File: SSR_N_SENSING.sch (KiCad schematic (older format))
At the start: 26 parts, among them P4 CONN_01X03, P7 CONN_01X02, P8 CONN_01X02, Q1 BC850, U10 ACS722, U3 SHARPS202S02, U4 ACS716

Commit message: PWR layout
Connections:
- net labels added: 230VPHASE
- net labels removed: 220VPHASE
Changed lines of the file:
@@
 CURR_SENSE_FILTERED
 Text GLabel 4200 2500 2    60   Input ~ 0
-220VPHASE
+230VPHASE
 $Comp
 L ACS722 U10

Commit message: almost ready
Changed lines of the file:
@@
 	1    0    0    -1
 $EndComp
-Wire Wire Line
-	3450 3200 3450 4350
-Connection ~ 3450 3300
-Connection ~ 3450 3400
-Wire Wire Line
-	3450 2500 3450 3100
-Connection ~ 3450 3000
-Connection ~ 3450 2900
-Connection ~ 3450 2800
-Wire Wire Line
-	3450 2400 4200 2400
 $Comp
 L R R13
@@
 	0    1    1    0
 $EndComp
-Wire Wire Line
-	3450 2500 3500 2500
-Wire Wire Line
-	3800 2500 3850 2500
-Wire Wire Line
-	4150 2500 4200 2500
 $Comp
 L GNDREF #PWR038
@@
 	0    1    1    0
 $EndComp
-Wire Wire Line
-	4200 2500 4200 2400
-Wire Wire Line
-	3450 2200 3550 2200
 $Comp
 L GNDREF #PWR040
@@
 	-1   0    0    1
 $EndComp
-Wire Wire Line
-	3550 2200 3550 2000
-Wire Wire Line
-	3550 2000 3700 2000
 $Comp
 L D D6
@@
 	0    -1   -1   0
 $EndComp
-Wire Wire Line
-	3650 2300 3450 2300
 $Comp
 L R R14
@@
 	-1   0    0    1
 $EndComp
-Wire Wire Line
-	4950 2900 5850 2900
-Connection ~ 5700 2900
-Wire Wire Line
-	4950 2900 4950 3000
 $Comp
 L GNDREF #PWR042
@@
 	1    0    0    -1
 $EndComp
-Wire Wire Line
-	5550 3300 4950 3300
 $Comp
 L C C11
@@
 	1    0    0    -1
 $EndComp
-Wire Wire Line
-	5300 3400 4950 3400
 Text HLabel 4950 2800 2    60   Input ~ 0
 FAULT_EN
 Text HLabel 4950 3100 2    60   Input ~ 0
 !FAULT
-Wire Wire Line
-	4950 3200 6250 3200
 $Comp
 L D D7
@@
 	1    0    0    -1
 $EndComp
-Wire Wire Line
-	6100 3500 6350 3500
-Connection ~ 6200 3500
 $Comp
 L GNDREF #PWR045
@@
 	1    0    0    -1
 $EndComp
-Wire Wire Line
-	6200 3800 6350 3800
-Wire Wire Line
-	6350 3800 6350 3900
 Text HLabel 6350 3500 2    60   Input ~ 0
 CURR_SENSE_FILTERED
@@
 	1    0    0    -1
 $EndComp
-Wire Wire Line
-	3450 4450 3450 4550
-Connection ~ 3450 3500
-Connection ~ 3450 4250
 $Comp
 L GNDREF #PWR046
@@
 	1    0    0    -1
 $EndComp
-Wire Wire Line
-	4950 4250 7400 4250
 $Comp
 L C C22
@@
 	1    0    0    -1
 $EndComp
-Wire Wire Line
-	6100 5050 6350 5050
-Connection ~ 6200 5050
 $Comp
 L GNDREF #PWR050
@@
 	1    0    0    -1
 $EndComp
-Wire Wire Line
-	6200 5350 6350 5350
-Wire Wire Line
-	6350 5350 6350 5450
 Text HLabel 6350 5050 2    60   Input ~ 0
 CURR_SENSE_FILTERED_2
@@
 	1    0    0    -1
 $EndComp
-Wire Wire Line
-	4950 4450 5150 4450
 $Comp
 L GNDREF #PWR051
@@
 	1    0    0    -1
 $EndComp
-Text HLabel 6300 4750 2    60   Input ~ 0
+Text HLabel 6100 4700 2    60   Input ~ 0
 CURR_SENSE_DIRECT_2
 $Comp
@@
 	1    0    0    -1
 $EndComp
-Wire Wire Line
-	4950 4350 5700 4350
-Connection ~ 5450 4350
-Wire Wire Line
-	5700 4650 5700 4750
-Wire Wire Line
-	5700 4700 6100 4700
-Connection ~ 5700 4700
-Wire Wire Line
-	6100 4700 6100 4750
 $Comp
 L CONN_01X02 P7
@@
 	-1   0    0    1
 $EndComp
-Wire Wire Line
-	3450 3100 3300 3100
-Wire Wire Line
-	3300 3200 3450 3200
 $Comp
 L CONN_01X02 P8
@@
 $EndComp
 Wire Wire Line
+	3450 3200 3450 4350
+Connection ~ 3450 3300
+Connection ~ 3450 3400
+Wire Wire Line
+	3450 2500 3450 3100
+Connection ~ 3450 3000
+Connection ~ 3450 2900
+Connection ~ 3450 2800
+Wire Wire Line
+	3450 2400 4200 2400
+Wire Wire Line
+	3450 2500 3500 2500
+Wire Wire Line
+	3800 2500 3850 2500
+Wire Wire Line
+	4150 2500 4200 2500
+Wire Wire Line
+	4200 2500 4200 2400
+Wire Wire Line
+	3450 2200 3550 2200
+Wire Wire Line
+	3550 2200 3550 2000
+Wire Wire Line
+	3550 2000 3700 2000
+Wire Wire Line
+	3650 2300 3450 2300
+Wire Wire Line
+	4950 2900 5850 2900
+Connection ~ 5700 2900
+Wire Wire Line
+	4950 2900 4950 3000
+Wire Wire Line
+	5550 3300 4950 3300
+Wire Wire Line
+	5300 3400 4950 3400
+Wire Wire Line
+	6100 3500 6350 3500
+Connection ~ 6200 3500
+Wire Wire Line
+	6200 3800 6350 3800
+Wire Wire Line
+	6350 3800 6350 3900
+Wire Wire Line
+	3450 4450 3450 4550
+Connection ~ 3450 3500
+Connection ~ 3450 4250
+Wire Wire Line
+	4950 4250 7400 4250
+Wire Wire Line
+	6100 5050 6350 5050
+Connection ~ 6200 5050
+Wire Wire Line
+	6200 5350 6350 5350
+Wire Wire Line
+	6350 5350 6350 5450
+Wire Wire Line
+	4950 4450 5150 4450
+Wire Wire Line
+	4950 4350 5700 4350
+Connection ~ 5450 4350
+Wire Wire Line
+	5700 4650 5700 4750
+Wire Wire Line
+	5700 4700 6100 4700
+Connection ~ 5700 4700
+Wire Wire Line
+	6100 4700 6100 4750
+Wire Wire Line
+	3450 3100 3300 3100
+Wire Wire Line
+	3300 3200 3450 3200
+Wire Wire Line
 	3450 4350 3300 4350
 Wire Wire Line
 	3300 4450 3450 4450
+Connection ~ 3650 2000
+Wire Wire Line
+	4950 3200 6250 3200
+Connection ~ 6100 3200
 $EndSCHEMATC

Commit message: maybe final
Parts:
- D6, D7, D8: footprint Diodes_SMD:DO-214AB_Handsoldering -> Diodes_SMD:SOD-123
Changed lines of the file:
@@
 F 0 "D6" H 3650 2250 50  0000 C CNN
 F 1 "D" H 3650 2050 50  0000 C CNN
-F 2 "Diodes_SMD:DO-214AB_Handsoldering" H 3650 2150 60  0001 C CNN
+F 2 "Diodes_SMD:SOD-123" H 3650 2150 60  0001 C CNN
 F 3 "" H 3650 2150 60  0000 C CNN
 	1    3650 2150
@@
 F 0 "D7" H 6100 3450 50  0000 C CNN
 F 1 "D" H 6100 3250 50  0000 C CNN
-F 2 "Diodes_SMD:DO-214AB_Handsoldering" H 6100 3350 60  0001 C CNN
+F 2 "Diodes_SMD:SOD-123" H 6100 3350 60  0001 C CNN
 F 3 "" H 6100 3350 60  0000 C CNN
 	1    6100 3350
@@
 F 0 "D8" H 6100 5000 50  0000 C CNN
 F 1 "D" H 6100 4800 50  0000 C CNN
-F 2 "Diodes_SMD:DO-214AB_Handsoldering" H 6100 4900 60  0001 C CNN
+F 2 "Diodes_SMD:SOD-123" H 6100 4900 60  0001 C CNN
 F 3 "" H 6100 4900 60  0000 C CNN
 	1    6100 4900

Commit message: printed version
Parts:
- R13: footprint Resistors_ThroughHole:Resistor_Horizontal_RM25mm -> Resistors_ThroughHole:Resistor_Horizontal_RM10mm
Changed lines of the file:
@@
 F 0 "R13" V 3730 2500 50  0000 C CNN
 F 1 "R_SNUB" V 3650 2500 50  0000 C CNN
-F 2 "Resistors_ThroughHole:Resistor_Horizontal_RM25mm" V 3580 2500 30  0001 C CNN
+F 2 "Resistors_ThroughHole:Resistor_Horizontal_RM10mm" V 3580 2500 30  0001 C CNN
 F 3 "" H 3650 2500 30  0000 C CNN
 	1    3650 2500

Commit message: save
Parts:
- removed C11, C12, C13, C14: C, Capacitors_SMD:C_1206_HandSoldering, symbol C
- removed D7: D, Diodes_SMD:SOD-123, symbol D
- removed P7: CONN_01X02, libs:PIN_CONN_0.3Inch, symbol CONN_01X02
- removed R16: R, Resistors_SMD:R_1206_HandSoldering, symbol R
- removed U4: ACS716, libs:ACS716, symbol ACS716
- C20: value C -> 10uF
- C21: value C -> 1nF
- C22: value C -> 0; footprint Capacitors_SMD:C_1206_HandSoldering -> 0
- C23: value C -> 10uF; footprint Capacitors_SMD:C_1206_HandSoldering -> 10uF
- R14: value R -> 150
- R15: value R -> 1k
- R17: value R -> 2k
- R18: value R -> 3k
- R19: value R -> 100k; footprint Resistors_SMD:R_1206_HandSoldering -> 100k
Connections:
- net labels removed: !FAULT, CURR_SENSE_DIRECT, CURR_SENSE_FILTERED, FAULT_EN
- wire segments 33 -> 22
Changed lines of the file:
@@
 EESchema Schematic File Version 2
+LIBS:viztisztito-rescue
 LIBS:power
 LIBS:device
@@
 MOTOR+
 $Comp
-L ACS716 U4
-U 1 1 561BA190
-P 4200 3150
-F 0 "U4" H 4200 3050 50  0000 C CNN
-F 1 "ACS716" H 4200 3250 50  0000 C CNN
-F 2 "libs:ACS716" H 4200 3150 50  0001 C CNN
-F 3 "DOCUMENTATION" H 4200 3150 50  0001 C CNN
-	1    4200 3150
-	1    0    0    -1
-$EndComp
-$Comp
 L R R13
 U 1 1 561BB7FA
@@
 $EndComp
 $Comp
-L GNDREF #PWR038
-U 1 1 561BB966
-P 4950 3500
-F 0 "#PWR038" H 4950 3250 50  0001 C CNN
-F 1 "GNDREF" H 4950 3350 50  0000 C CNN
-F 2 "" H 4950 3500 60  0000 C CNN
-F 3 "" H 4950 3500 60  0000 C CNN
-	1    4950 3500
-	1    0    0    -1
-$EndComp
-$Comp
-L +3.3V #PWR039
-U 1 1 561BB9CA
-P 5850 2900
-F 0 "#PWR039" H 5850 2750 50  0001 C CNN
-F 1 "+3.3V" H 5850 3040 50  0000 C CNN
-F 2 "" H 5850 2900 60  0000 C CNN
-F 3 "" H 5850 2900 60  0000 C CNN
-	1    5850 2900
-	0    1    1    0
-$EndComp
-$Comp
 L GNDREF #PWR040
 U 1 1 561BC35A
@@
 P 3800 2300
 F 0 "R14" V 3880 2300 50  0000 C CNN
-F 1 "R" V 3800 2300 50  0000 C CNN
+F 1 "150" V 3800 2300 50  0000 C CNN
 F 2 "Resistors_SMD:R_1206_HandSoldering" V 3730 2300 30  0001 C CNN
 F 3 "" H 3800 2300 30  0000 C CNN
@@
 P 4150 1800
 F 0 "R15" V 4230 1800 50  0000 C CNN
-F 1 "R" V 4150 1800 50  0000 C CNN
+F 1 "1k" V 4150 1800 50  0000 C CNN
 F 2 "Resistors_SMD:R_1206_HandSoldering" V 4080 1800 30  0001 C CNN
 F 3 "" H 4150 1800 30  0000 C CNN
@@
 	-1   0    0    1
 $EndComp
-Text HLabel 6250 3200 2    60   Input ~ 0
-CURR_SENSE_DIRECT
-$Comp
-L C C13
-U 1 1 561BD266
-P 5700 2750
-F 0 "C13" H 5725 2850 50  0000 L CNN
-F 1 "C" H 5725 2650 50  0000 L CNN
-F 2 "Capacitors_SMD:C_1206_HandSoldering" H 5738 2600 30  0001 C CNN
-F 3 "" H 5700 2750 60  0000 C CNN
-	1    5700 2750
-	-1   0    0    1
-$EndComp
-$Comp
-L GNDREF #PWR042
-U 1 1 561BD41D
-P 5700 2600
-F 0 "#PWR042" H 5700 2350 50  0001 C CNN
-F 1 "GNDREF" H 5700 2450 50  0000 C CNN
-F 2 "" H 5700 2600 60  0000 C CNN
-F 3 "" H 5700 2600 60  0000 C CNN
-	1    5700 2600
-	-1   0    0    1
-$EndComp
-$Comp
-L C C12
-U 1 1 561BD44D
-P 5550 3450
-F 0 "C12" H 5575 3550 50  0000 L CNN
-F 1 "C" H 5575 3350 50  0000 L CNN
-F 2 "Capacitors_SMD:C_1206_HandSoldering" H 5588 3300 30  0001 C CNN
-F 3 "" H 5550 3450 60  0000 C CNN
-	1    5550 3450
-	1    0    0    -1
-$EndComp
-$Comp
-L GNDREF #PWR043
-U 1 1 561BD495
-P 5550 3600
-F 0 "#PWR043" H 5550 3350 50  0001 C CNN
-F 1 "GNDREF" H 5550 3450 50  0000 C CNN
-F 2 "" H 5550 3600 60  0000 C CNN
-F 3 "" H 5550 3600 60  0000 C CNN
-	1    5550 3600
-	1    0    0    -1
-$EndComp
-$Comp
-L C C11
-U 1 1 561BD4EE
-P 5300 3550
-F 0 "C11" H 5325 3650 50  0000 L CNN
-F 1 "C" H 5325 3450 50  0000 L CNN
-F 2 "Capacitors_SMD:C_1206_HandSoldering" H 5338 3400 30  0001 C CNN
-F 3 "" H 5300 3550 60  0000 C CNN
-	1    5300 3550
-	1    0    0    -1
-$EndComp
-$Comp
-L GNDREF #PWR044
-U 1 1 561BD527
-P 5300 3700
-F 0 "#PWR044" H 5300 3450 50  0001 C CNN
-F 1 "GNDREF" H 5300 3550 50  0000 C CNN
-F 2 "" H 5300 3700 60  0000 C CNN
-F 3 "" H 5300 3700 60  0000 C CNN
-	1    5300 3700
-	1    0    0    -1
-$EndComp
-Text HLabel 4950 2800 2    60   Input ~ 0
-FAULT_EN
-Text HLabel 4950 3100 2    60   Input ~ 0
-!FAULT
-$Comp
-L D D7
-U 1 1 561BF7C0
-P 6100 3350
-F 0 "D7" H 6100 3450 50  0000 C CNN
-F 1 "D" H 6100 3250 50  0000 C CNN
-F 2 "Diodes_SMD:SOD-123" H 6100 3350 60  0001 C CNN
-F 3 "" H 6100 3350 60  0000 C CNN
-	1    6100 3350
-	0    -1   -1   0
-$EndComp
-$Comp
-L R R16
-U 1 1 561BF888
-P 6200 3650
-F 0 "R16" V 6280 3650 50  0000 C CNN
-F 1 "R" V 6200 3650 50  0000 C CNN
-F 2 "Resistors_SMD:R_1206_HandSoldering" V 6130 3650 30  0001 C CNN
-F 3 "" H 6200 3650 30  0000 C CNN
-	1    6200 3650
-	-1   0    0    1
-$EndComp
-$Comp
-L C C14
-U 1 1 561BF95E
-P 6350 3650
-F 0 "C14" H 6375 3750 50  0000 L CNN
-F 1 "C" H 6375 3550 50  0000 L CNN
-F 2 "Capacitors_SMD:C_1206_HandSoldering" H 6388 3500 30  0001 C CNN
-F 3 "" H 6350 3650 60  0000 C CNN
-	1    6350 3650
-	1    0    0    -1
-$EndComp
-$Comp
-L GNDREF #PWR045
-U 1 1 561BFC0A
-P 6350 3900
-F 0 "#PWR045" H 6350 3650 50  0001 C CNN
-F 1 "GNDREF" H 6350 3750 50  0000 C CNN
-F 2 "" H 6350 3900 60  0000 C CNN
-F 3 "" H 6350 3900 60  0000 C CNN
-	1    6350 3900
-	1    0    0    -1
-$EndComp
-Text HLabel 6350 3500 2    60   Input ~ 0
-CURR_SENSE_FILTERED
 Text GLabel 4200 2500 2    60   Input ~ 0
 230VPHASE
@@
 P 4950 4100
 F 0 "C20" H 4975 4200 50  0000 L CNN
-F 1 "C" H 4975 4000 50  0000 L CNN
+F 1 "10uF" H 4975 4000 50  0000 L CNN
 F 2 "Capacitors_SMD:C_1206_HandSoldering" H 4988 3950 30  0001 C CNN
 F 3 "" H 4950 4100 60  0000 C CNN
@@
 P 5450 4500
 F 0 "C22" H 5475 4600 50  0000 L CNN
-F 1 "C" H 5475 4400 50  0000 L CNN
-F 2 "Capacitors_SMD:C_1206_HandSoldering" H 5488 4350 30  0001 C CNN
+F 1 "0" H 5475 4400 50  0000 L CNN
+F 2 "0" H 5488 4350 30  0001 C CNN
 F 3 "" H 5450 4500 60  0000 C CNN
 	1    5450 4500
@@
 P 6200 5200
 F 0 "R19" V 6280 5200 50  0000 C CNN
-F 1 "R" V 6200 5200 50  0000 C CNN
-F 2 "Resistors_SMD:R_1206_HandSoldering" V 6130 5200 30  0001 C CNN
+F 1 "100k" V 6200 5200 50  0000 C CNN
+F 2 "100k" V 6130 5200 30  0001 C CNN
 F 3 "" H 6200 5200 30  0000 C CNN
 	1    6200 5200
@@
 P 6350 5200
 F 0 "C23" H 6375 5300 50  0000 L CNN
-F 1 "C" H 6375 5100 50  0000 L CNN
-F 2 "Capacitors_SMD:C_1206_HandSoldering" H 6388 5050 30  0001 C CNN
+F 1 "10uF" H 6375 5100 50  0000 L CNN
+F 2 "10uF" H 6388 5050 30  0001 C CNN
 F 3 "" H 6350 5200 60  0000 C CNN
 	1    6350 5200
@@
 P 5150 4600
 F 0 "C21" H 5175 4700 50  0000 L CNN
-F 1 "C" H 5175 4500 50  0000 L CNN
+F 1 "1nF" H 5175 4500 50  0000 L CNN
 F 2 "Capacitors_SMD:C_1206_HandSoldering" H 5188 4450 30  0001 C CNN
 F 3 "" H 5150 4600 60  0000 C CNN
@@
 P 5700 4500
 F 0 "R17" V 5780 4500 50  0000 C CNN
-F 1 "R" V 5700 4500 50  0000 C CNN
+F 1 "2k" V 5700 4500 50  0000 C CNN
 F 2 "Resistors_SMD:R_1206_HandSoldering" V 5630 4500 30  0001 C CNN
 F 3 "" H 5700 4500 30  0000 C CNN
@@
 P 5700 4900
 F 0 "R18" V 5780 4900 50  0000 C CNN
-F 1 "R" V 5700 4900 50  0000 C CNN
+F 1 "3k" V 5700 4900 50  0000 C CNN
 F 2 "Resistors_SMD:R_1206_HandSoldering" V 5630 4900 30  0001 C CNN
 F 3 "" H 5700 4900 30  0000 C CNN
@@
 $EndComp
 $Comp
-L CONN_01X02 P7
-U 1 1 5626DC35
-P 3100 3150
-F 0 "P7" H 3100 3300 50  0000 C CNN
-F 1 "CONN_01X02" V 3200 3150 50  0000 C CNN
-F 2 "libs:PIN_CONN_0.3Inch" H 3100 3150 60  0000 C CNN
-F 3 "" H 3100 3150 60  0000 C CNN
-	1    3100 3150
-	-1   0    0    1
-$EndComp
-$Comp
 L CONN_01X02 P8
 U 1 1 5626DE5E
@@
 $EndComp
 Wire Wire Line
-	3450 3200 3450 4350
-Connection ~ 3450 3300
-Connection ~ 3450 3400
-Wire Wire Line
-	3450 2500 3450 3100
-Connection ~ 3450 3000
-Connection ~ 3450 2900
-Connection ~ 3450 2800
-Wire Wire Line
 	3450 2400 4200 2400
 Wire Wire Line
@@
 	3650 2300 3450 2300
 Wire Wire Line
-	4950 2900 5850 2900
-Connection ~ 5700 2900
-Wire Wire Line
-	4950 2900 4950 3000
-Wire Wire Line
-	5550 3300 4950 3300
-Wire Wire Line
-	5300 3400 4950 3400
-Wire Wire Line
-	6100 3500 6350 3500
-Connection ~ 6200 3500
-Wire Wire Line
-	6200 3800 6350 3800
-Wire Wire Line
-	6350 3800 6350 3900
-Wire Wire Line
 	3450 4450 3450 4550
-Connection ~ 3450 3500
 Connection ~ 3450 4250
 Wire Wire Line
@@
 	6100 4700 6100 4750
 Wire Wire Line
-	3450 3100 3300 3100
-Wire Wire Line
-	3300 3200 3450 3200
-Wire Wire Line
 	3450 4350 3300 4350
 Wire Wire Line
@@
 Connection ~ 3650 2000
 Wire Wire Line
-	4950 3200 6250 3200
-Connection ~ 6100 3200
+	3450 4250 3450 2500
 $EndSCHEMATC

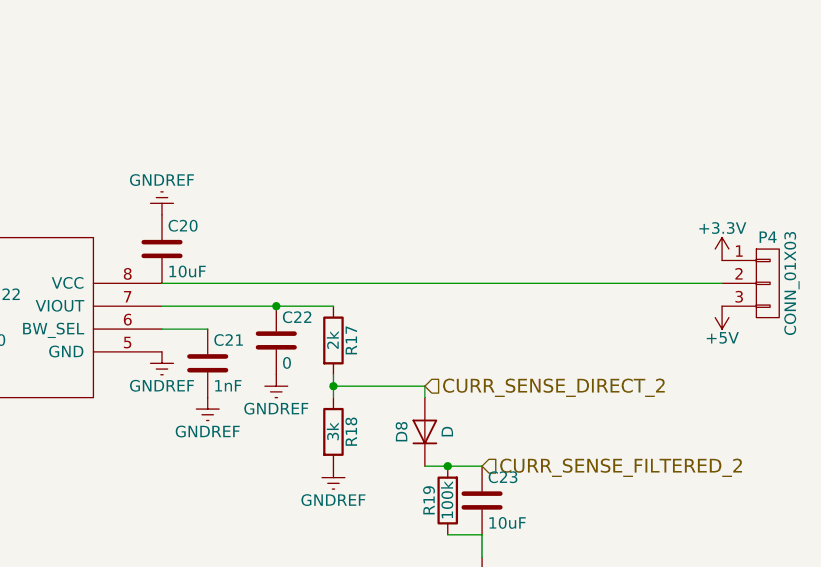
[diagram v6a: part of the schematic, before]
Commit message: new layout, added psu
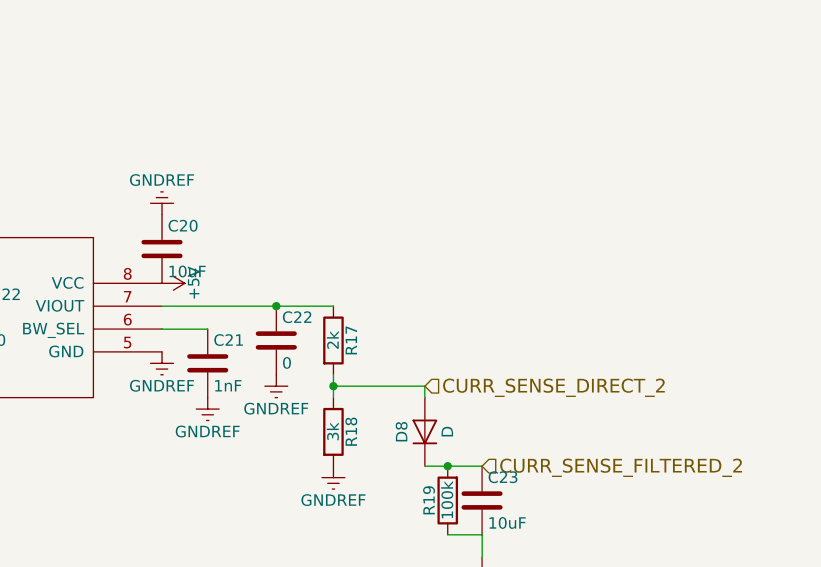
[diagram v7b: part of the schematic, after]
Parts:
- removed P4: CONN_01X03, Socket_Strips:Socket_Strip_Straight_1x03, symbol CONN_01X03
- C22: footprint 0 -> Capacitors_SMD:C_1206_HandSoldering
- C23: footprint 10uF -> Capacitors_SMD:C_1206_HandSoldering
- R19: footprint 100k -> Resistors_SMD:R_1206_HandSoldering
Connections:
- net +5V: now also C20.2, U10.8 (VCC)
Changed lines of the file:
@@
 LIBS:contrib
 LIBS:valves
-LIBS:mylib
+LIBS:analog_devices
+LIBS:libs
 LIBS:viztisztito-cache
 EELAYER 25 0
@@
 $EndComp
 $Comp
-L GNDREF #PWR040
+L GNDREF #PWR026
 U 1 1 561BC35A
 P 3700 1600
-F 0 "#PWR040" H 3700 1350 50  0001 C CNN
+F 0 "#PWR026" H 3700 1350 50  0001 C CNN
 F 1 "GNDREF" H 3700 1450 50  0000 C CNN
 F 2 "" H 3700 1600 60  0000 C CNN
@@
 $EndComp
 $Comp
-L +3.3V #PWR041
+L +3.3V #PWR027
 U 1 1 561BC509
 P 3950 2300
-F 0 "#PWR041" H 3950 2150 50  0001 C CNN
+F 0 "#PWR027" H 3950 2150 50  0001 C CNN
 F 1 "+3.3V" H 3950 2440 50  0000 C CNN
 F 2 "" H 3950 2300 60  0000 C CNN
@@
 $EndComp
 $Comp
-L GNDREF #PWR046
+L GNDREF #PWR028
 U 1 1 5625123B
 P 4950 4550
-F 0 "#PWR046" H 4950 4300 50  0001 C CNN
+F 0 "#PWR028" H 4950 4300 50  0001 C CNN
 F 1 "GNDREF" H 4950 4400 50  0000 C CNN
 F 2 "" H 4950 4550 60  0000 C CNN
@@
 $EndComp
 $Comp
-L GNDREF #PWR047
+L GNDREF #PWR029
 U 1 1 56251330
 P 4950 3950
-F 0 "#PWR047" H 4950 3700 50  0001 C CNN
+F 0 "#PWR029" H 4950 3700 50  0001 C CNN
 F 1 "GNDREF" H 4950 3800 50  0000 C CNN
 F 2 "" H 4950 3950 60  0000 C CNN
@@
 	1    4950 3950
 	-1   0    0    1
-$EndComp
-$Comp
-L +3.3V #PWR048
-U 1 1 5625147B
-P 7400 4150
-F 0 "#PWR048" H 7400 4000 50  0001 C CNN
-F 1 "+3.3V" H 7400 4290 50  0000 C CNN
-F 2 "" H 7400 4150 60  0000 C CNN
-F 3 "" H 7400 4150 60  0000 C CNN
-	1    7400 4150
-	1    0    0    -1
 $EndComp
 $Comp
@@
 F 0 "C22" H 5475 4600 50  0000 L CNN
 F 1 "0" H 5475 4400 50  0000 L CNN
-F 2 "0" H 5488 4350 30  0001 C CNN
+F 2 "Capacitors_SMD:C_1206_HandSoldering" H 5488 4350 30  0001 C CNN
 F 3 "" H 5450 4500 60  0000 C CNN
 	1    5450 4500
@@
 $EndComp
 $Comp
-L GNDREF #PWR049
+L GNDREF #PWR030
 U 1 1 5625160B
 P 5450 4650
-F 0 "#PWR049" H 5450 4400 50  0001 C CNN
+F 0 "#PWR030" H 5450 4400 50  0001 C CNN
 F 1 "GNDREF" H 5450 4500 50  0000 C CNN
 F 2 "" H 5450 4650 60  0000 C CNN
@@
 F 0 "R19" V 6280 5200 50  0000 C CNN
 F 1 "100k" V 6200 5200 50  0000 C CNN
-F 2 "100k" V 6130 5200 30  0001 C CNN
+F 2 "Resistors_SMD:R_1206_HandSoldering" V 6130 5200 30  0001 C CNN
 F 3 "" H 6200 5200 30  0000 C CNN
 	1    6200 5200
@@
 F 0 "C23" H 6375 5300 50  0000 L CNN
 F 1 "10uF" H 6375 5100 50  0000 L CNN
-F 2 "10uF" H 6388 5050 30  0001 C CNN
+F 2 "Capacitors_SMD:C_1206_HandSoldering" H 6388 5050 30  0001 C CNN
 F 3 "" H 6350 5200 60  0000 C CNN
 	1    6350 5200
@@
 $EndComp
 $Comp
-L GNDREF #PWR050
+L GNDREF #PWR031
 U 1 1 562518AC
 P 6350 5450
-F 0 "#PWR050" H 6350 5200 50  0001 C CNN
+F 0 "#PWR031" H 6350 5200 50  0001 C CNN
 F 1 "GNDREF" H 6350 5300 50  0000 C CNN
 F 2 "" H 6350 5450 60  0000 C CNN
@@
 $EndComp
 $Comp
-L GNDREF #PWR051
+L GNDREF #PWR032
 U 1 1 56251B91
 P 5150 4750
-F 0 "#PWR051" H 5150 4500 50  0001 C CNN
+F 0 "#PWR032" H 5150 4500 50  0001 C CNN
 F 1 "GNDREF" H 5150 4600 50  0000 C CNN
 F 2 "" H 5150 4750 60  0000 C CNN
@@
 CURR_SENSE_DIRECT_2
 $Comp
-L CONN_01X03 P4
-U 1 1 56254CF7
-P 7600 4250
-F 0 "P4" H 7600 4450 50  0000 C CNN
-F 1 "CONN_01X03" V 7700 4250 50  0000 C CNN
-F 2 "Socket_Strips:Socket_Strip_Straight_1x03" H 7600 4250 60  0001 C CNN
-F 3 "" H 7600 4250 60  0000 C CNN
-	1    7600 4250
-	1    0    0    -1
-$EndComp
-$Comp
-L +5V #PWR052
+L +5V #PWR033
 U 1 1 56254E82
-P 7400 4350
-F 0 "#PWR052" H 7400 4200 50  0001 C CNN
-F 1 "+5V" H 7400 4490 50  0000 C CNN
-F 2 "" H 7400 4350 60  0000 C CNN
-F 3 "" H 7400 4350 60  0000 C CNN
-	1    7400 4350
-	-1   0    0    1
+P 4950 4250
+F 0 "#PWR033" H 4950 4100 50  0001 C CNN
+F 1 "+5V" H 4950 4390 50  0000 C CNN
+F 2 "" H 4950 4250 60  0000 C CNN
+F 3 "" H 4950 4250 60  0000 C CNN
+	1    4950 4250
+	0    1    1    0
 $EndComp
 $Comp
@@
 $EndComp
 $Comp
-L GNDREF #PWR053
+L GNDREF #PWR034
 U 1 1 56255BC2
 P 5700 5050
-F 0 "#PWR053" H 5700 4800 50  0001 C CNN
+F 0 "#PWR034" H 5700 4800 50  0001 C CNN
 F 1 "GNDREF" H 5700 4900 50  0000 C CNN
 F 2 "" H 5700 5050 60  0000 C CNN
@@
 Connection ~ 3450 4250
 Wire Wire Line
-	4950 4250 7400 4250
-Wire Wire Line
 	6100 5050 6350 5050

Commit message: small changes
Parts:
- P8: footprint libs:PIN_CONN_0.3Inch -> Fuse_Holders_and_Fuses:Fuseholder5x20_horiz_SemiClosed_Casing10x25mm
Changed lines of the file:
@@
 LIBS:valves
 LIBS:analog_devices
-LIBS:libs
 LIBS:viztisztito-cache
 EELAYER 25 0
@@
 F 0 "P8" H 3100 4550 50  0000 C CNN
 F 1 "CONN_01X02" V 3200 4400 50  0000 C CNN
-F 2 "libs:PIN_CONN_0.3Inch" H 3100 4400 60  0000 C CNN
+F 2 "Fuse_Holders_and_Fuses:Fuseholder5x20_horiz_SemiClosed_Casing10x25mm" H 3100 4400 60  0000 C CNN
 F 3 "" H 3100 4400 60  0000 C CNN
 	1    3100 4400
